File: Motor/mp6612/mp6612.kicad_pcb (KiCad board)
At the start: 4 copper layers, 34.2 x 34 mm, 32 parts, among them J1 Conn_01x07, J2 OQ0212500000G, J3 TB002-500-02BE, U1 MP6612DGF-P

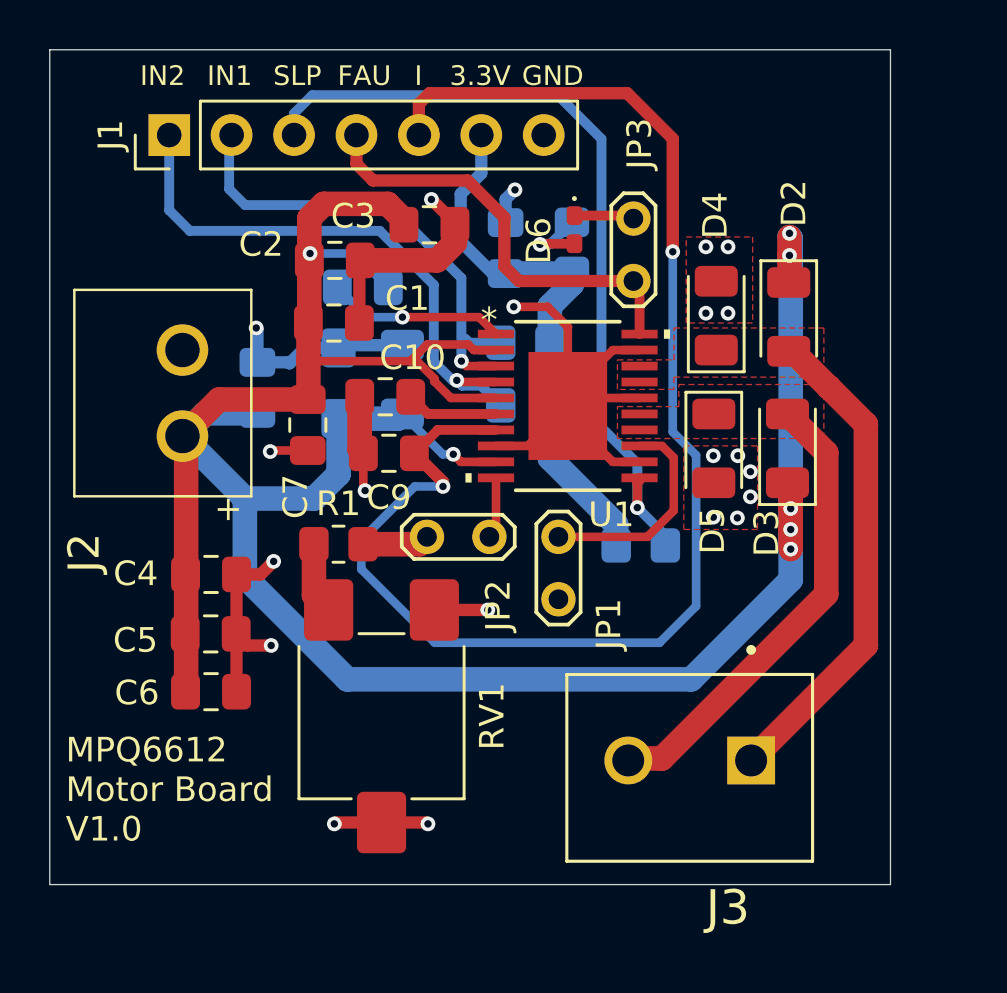
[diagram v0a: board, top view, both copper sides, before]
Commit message: Rename Project
Rename project to MP6612
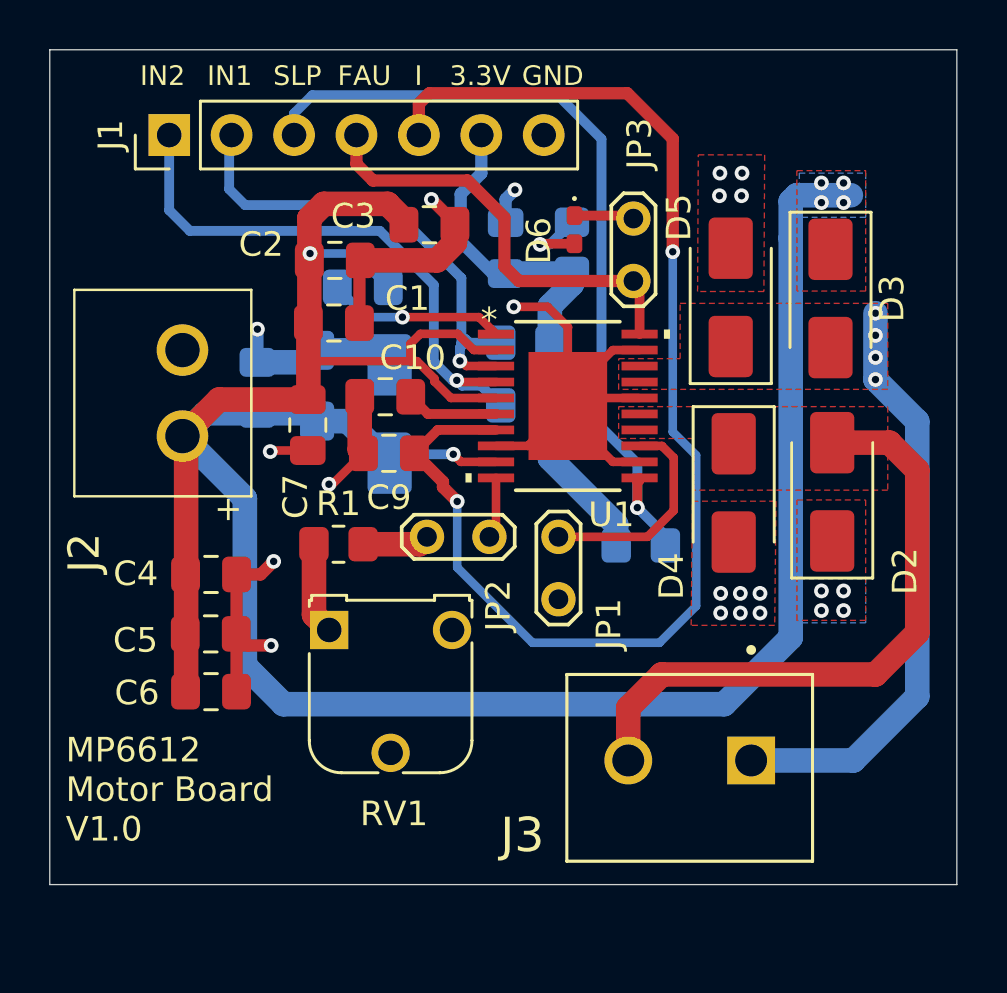
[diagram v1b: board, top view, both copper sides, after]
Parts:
- D1, D2, D3, D4, D5: value D -> B340A; footprint Diode_SMD:D_1206_3216Metric -> Diode_SMD:D_SMA
- RV1: footprint Potentiometer_SMD:Potentiometer_ACP_CA6-VSMD_Vertical -> Potentiometer_THT:Potentiometer_Runtron_RM-065_Vertical
- moved D2 7.33 mm to (170.8, 90.2), turned to 90 degrees
- moved D4 7.25 mm to (166.8, 90.2), turned to -90 degrees
- moved D3 6.35 mm to (170.8, 82.3), turned to -90 degrees
- moved D5 6.18 mm to (166.7, 82.3), turned to 90 degrees
- moved RV1 4.11 mm to (150.4, 95.8), turned to 0 degrees
- moved D1 1.49 mm to (152.8, 87.0)
- moved C8 0.88 mm to (149.9, 85.8)
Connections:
- D2 pad 2: /Out1 -> /Out2
- D3 pad 2: /Out2 -> /Out1
- D4 pad 1: /Out1 -> /Out2
- D5 pad 1: /Out2 -> /Out1
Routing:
- net /Out2: track 18.7 -> 25.7 mm
- net GND: track 58.3 -> 52.2 mm, vias 21 -> 18
- net /visen: track 58.4 -> 52.6 mm
- net /Out1: track 19.9 -> 24.1 mm, vias 0 -> 4
- net Net-(R1-Pad1): track 2.92 -> 3.75 mm
- net /Vin: track 111.7 -> 112.3 mm, vias 7 -> 10
- added copper zone on B.Cu, net /Vin
- added copper zone on F.Cu, net /Vin
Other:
- board size 34.2 x 34 mm -> 36.9 x 34 mm
- board text added: "JP1 OVER CURRENT JP2 CURRENT SET JP3 LED FAULT"
- board text added: "MP6612 Motor Board V1.0"
- board text removed: "JP1 OVER CURRENT ADJ JP2 CURRENT SET JP3 LED FAULT"
- board text removed: "MPQ6612 Motor Board V1.0"
